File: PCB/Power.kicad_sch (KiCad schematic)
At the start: 32 parts, among them J1 3.7v LiPo, Q1 MMBT2907ALT1HTSA1, Q2 NMOS, U1 TPS61090, U2 LD1117S33TR_SOT223, U3 MCP73831T-2ACI/OT, U6 MAX17048G

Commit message: fixed schematic errors
Accidentally set all SMD 0603 to SMD 0603 metric
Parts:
- C1, C16, C2, C4, C5, C6: footprint Capacitor_SMD:C_0201_0603Metric -> Capacitor_SMD:C_0603_1608Metric
- D1, D2: footprint LED_SMD:LED_0201_0603Metric -> LED_SMD:LED_0603_1608Metric
- R1, R11, R12, R2, R23, R3, R4, R5, R6, R7, R8, R9: footprint Resistor_SMD:R_0201_0603Metric -> Resistor_SMD:R_0603_1608Metric
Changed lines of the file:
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@@
 			)
 		)
-		(property "Footprint" "Resistor_SMD:R_0201_0603Metric"
+		(property "Footprint" "Resistor_SMD:R_0603_1608Metric"
 			(at 48.26 154.178 90)
 			(effects
@@
 			)
 		)
-		(property "Footprint" "Resistor_SMD:R_0201_0603Metric"
+		(property "Footprint" "Resistor_SMD:R_0603_1608Metric"
 			(at 98.552 168.91 90)
 			(effects
@@
 			)
 		)
-		(property "Footprint" "Capacitor_SMD:C_0201_0603Metric"
+		(property "Footprint" "Capacitor_SMD:C_0603_1608Metric"
 			(at 229.5652 72.39 0)
 			(effects
@@
 			)
 		)
-		(property "Footprint" "Capacitor_SMD:C_0201_0603Metric"
+		(property "Footprint" "Capacitor_SMD:C_0603_1608Metric"
 			(at 194.0052 121.92 0)
 			(effects
@@
 			)
 		)
-		(property "Footprint" "Capacitor_SMD:C_0201_0603Metric"
+		(property "Footprint" "Capacitor_SMD:C_0603_1608Metric"
 			(at 133.0452 49.53 0)
 			(effects
@@
 			)
 		)
-		(property "Footprint" "Capacitor_SMD:C_0201_0603Metric"
+		(property "Footprint" "Capacitor_SMD:C_0603_1608Metric"
 			(at 254.9652 72.39 0)
 			(effects
@@
 			)
 		)
-		(property "Footprint" "Resistor_SMD:R_0201_0603Metric"
+		(property "Footprint" "Resistor_SMD:R_0603_1608Metric"
 			(at 64.77 103.378 90)
 			(effects
@@
 			)
 		)
-		(property "Footprint" "Resistor_SMD:R_0201_0603Metric"
+		(property "Footprint" "Resistor_SMD:R_0603_1608Metric"
 			(at 126.492 180.34 90)
 			(effects
@@
 			)
 		)
-		(property "Footprint" "Resistor_SMD:R_0201_0603Metric"
+		(property "Footprint" "Resistor_SMD:R_0603_1608Metric"
 			(at 130.302 60.96 90)
 			(effects
@@
 			)
 		)
-		(property "Footprint" "Resistor_SMD:R_0201_0603Metric"
+		(property "Footprint" "Resistor_SMD:R_0603_1608Metric"
 			(at 87.122 72.39 90)
 			(effects
@@
 			)
 		)
-		(property "Footprint" "Resistor_SMD:R_0201_0603Metric"
+		(property "Footprint" "Resistor_SMD:R_0603_1608Metric"
 			(at 83.058 57.15 90)
 			(effects
@@
 			)
 		)
-		(property "Footprint" "Resistor_SMD:R_0201_0603Metric"
+		(property "Footprint" "Resistor_SMD:R_0603_1608Metric"
 			(at 130.302 68.58 90)
 			(effects
@@
 			)
 		)
-		(property "Footprint" "Capacitor_SMD:C_0201_0603Metric"
+		(property "Footprint" "Capacitor_SMD:C_0603_1608Metric"
 			(at 84.1248 48.26 0)
 			(effects
@@
 			)
 		)
-		(property "Footprint" "Resistor_SMD:R_0201_0603Metric"
+		(property "Footprint" "Resistor_SMD:R_0603_1608Metric"
 			(at 42.418 160.02 90)
 			(effects
@@
 			)
 		)
-		(property "Footprint" "Resistor_SMD:R_0201_0603Metric"
+		(property "Footprint" "Resistor_SMD:R_0603_1608Metric"
 			(at 87.122 62.23 90)
 			(effects
@@
 			)
 		)
-		(property "Footprint" "LED_SMD:LED_0201_0603Metric"
+		(property "Footprint" "LED_SMD:LED_0603_1608Metric"
 			(at 128.27 168.91 0)
 			(effects
@@
 			)
 		)
-		(property "Footprint" "Capacitor_SMD:C_0201_0603Metric"
+		(property "Footprint" "Capacitor_SMD:C_0603_1608Metric"
 			(at 109.5248 147.32 0)
 			(effects
@@
 			)
 		)
-		(property "Footprint" "Resistor_SMD:R_0201_0603Metric"
+		(property "Footprint" "Resistor_SMD:R_0603_1608Metric"
 			(at 47.752 88.9 90)
 			(effects
@@
 			)
 		)
-		(property "Footprint" "LED_SMD:LED_0201_0603Metric"
+		(property "Footprint" "LED_SMD:LED_0603_1608Metric"
 			(at 49.53 77.47 0)
 			(effects
@@
 			)
 		)
-		(property "Footprint" "Resistor_SMD:R_0201_0603Metric"
+		(property "Footprint" "Resistor_SMD:R_0603_1608Metric"
 			(at 248.158 134.62 90)
 			(effects

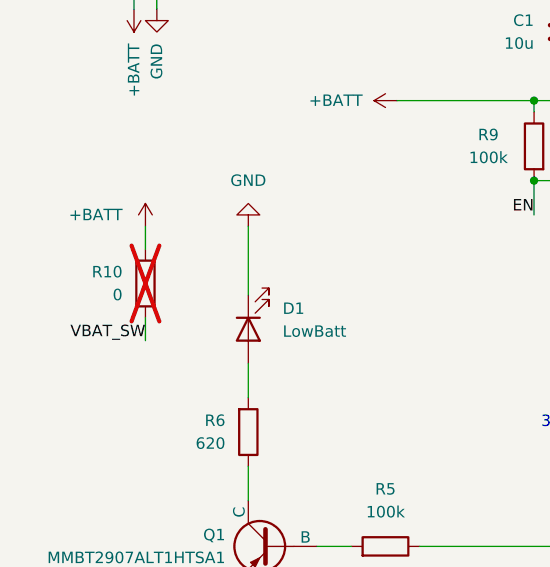
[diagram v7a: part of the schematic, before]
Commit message: Finished initial pcb routing
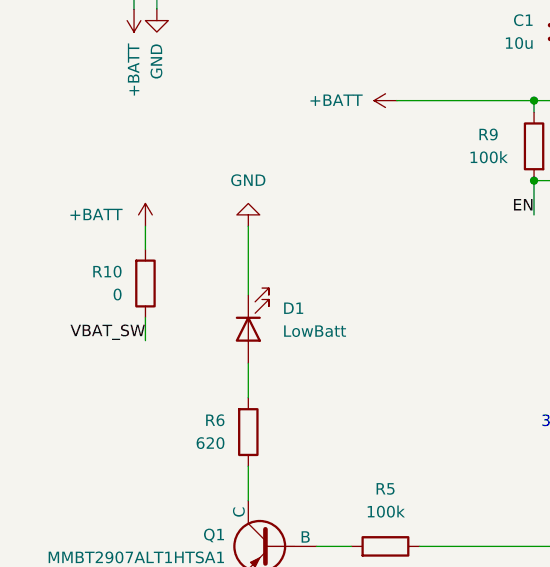
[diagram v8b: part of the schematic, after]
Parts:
- R10: footprint Resistor_SMD:R_0201_0603Metric -> Resistor_SMD:R_0603_1608Metric; now fitted; now in the parts list
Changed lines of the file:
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@@
 		(unit 1)
 		(exclude_from_sim no)
-		(in_bom no)
-		(on_board no)
-		(dnp yes)
+		(in_bom yes)
+		(on_board yes)
+		(dnp no)
 		(property "Reference" "R10"
 			(at 35.56 71.1199 0)
@@
 			)
 		)
-		(property "Footprint" "Resistor_SMD:R_0201_0603Metric"
+		(property "Footprint" "Resistor_SMD:R_0603_1608Metric"
 			(at 36.322 72.39 90)
 			(effects
